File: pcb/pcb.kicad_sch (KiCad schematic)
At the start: 249 parts, among them J1 USB_C_Receptacle_USB2.0, J2 AVR-ISP-6, SW1 1U, SW10 1U, SW100 ISO SHIFT, SW101 2U, SW102 1.25U CTRL, SW103 1.25U GUI, SW104 1.25U ALT, SW105 6.25u SPACE, SW106 1U ALT, SW107 1U GUI, SW108 1U CTRL, SW109 1U, SW11 1U, SW110 1U, SW111 1U, SW112 1U, SW113 1U, SW114 1U, SW115 1.5U CTRL, SW116 1U GUI, SW117 1.5U ALT, SW118 7U SPACE, SW119 1.5U ALT, SW12 1U, SW120 1.5U CTRL, SW121 1.5U GUI, SW122 6U SPACE, SW123 SW_Push, SW124 SW_Push, SW13 1U, SW14 1U, SW15 1U, SW16 1U, SW17 1U, SW18 1U, SW19 1U, SW2 1U, SW20 1U, SW21 1U, SW22 1U, SW23 1U, SW24 1U, SW25 1U, SW26 1U, SW27 1U, SW28 1U, SW29 1U, SW3 1U, SW30 1U, SW31 1U, SW32 1U, SW33 1U, SW34 1U, SW35 1U, SW36 1U, SW37 2U, SW38 1U, SW39 1U, SW4 1U, SW40 1U, SW41 1U, SW42 1U, SW43 1.5U, SW44 1U, SW45 1U, SW46 1U, SW47 1U, SW48 1U, SW49 1U, SW5 1U, SW50 1U, SW51 1U, SW52 1U, SW53 1U, SW54 1U, SW55 1U, SW56 1.5U, SW57 1U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

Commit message: Finished first routing attempt
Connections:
- net COL0: now also U1.20 (PD6)
- net COL1: now also U1.19 (PD5)
- net COL2: now also U1.15 (PD1)
- net COL3: now also U1.14 (PD0)
- net COL4: now also U1.21 (PD7)
- net ROW0: now also U1.29 (PC7)
- net ROW1: now also U1.28 (PC6)
- net ROW10: now also D89.1 (K), U1.35 (PA5)
- net ROW11: now also U1.36 (PA4)
- net ROW12: now also U1.37 (PA3)
- net ROW2: now also U1.33 (PA7)
- net ROW3: now also U1.27 (PC5)
- net ROW4: now also U1.26 (PC4)
- net ROW5: now also U1.25 (PC3)
- net ROW6: now also U1.24 (PC2)
- net ROW7: now also U1.23 (PC1)
- net ROW8: now also U1.22 (PC0)
- net ROW9: now also U1.34 (PA6)
- net at SW94.1: now also D89.2 (A)
- no-connect marks 3 -> 7
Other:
- moved on the sheet: D89
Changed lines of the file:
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@@
   (junction (at 167.64 140.97) (diameter 0) (color 0 0 0 0)
   )
+  (no_connect (at 35.56 224.79))
+  (no_connect (at 33.02 224.79))
+  (no_connect (at 30.48 224.79))
+  (no_connect (at -177.165 242.57))
   (no_connect (at 200.66 265.43))
   (no_connect (at 45.72 255.27))
@@
     )
   )
+  (global_label "ROW9" (shape input) (at 45.72 224.79 90) (fields_autoplaced)
+    (effects (font (size 1.27 1.27)) (justify left))
+    (property "Intersheet References" "${INTERSHEET_REFS}" (id 0) (at 45.6406 217.1155 90)
+      (effects (font (size 1.27 1.27)) (justify left) hide)
+    )
+  )
   (global_label "SCK" (shape input) (at 71.12 224.79 90) (fields_autoplaced)
     (effects (font (size 1.27 1.27)) (justify left))
@@
     )
   )
-  (global_label "COL1" (shape input) (at 50.165 215.9 90) (fields_autoplaced)
+  (global_label "COL1" (shape input) (at 111.76 224.79 90) (fields_autoplaced)
     (effects (font (size 1.27 1.27)) (justify left))
-    (property "Intersheet References" "${INTERSHEET_REFS}" (id 0) (at 50.0856 208.6488 90)
+    (property "Intersheet References" "${INTERSHEET_REFS}" (id 0) (at 111.6806 217.5388 90)
       (effects (font (size 1.27 1.27)) (justify left) hide)
     )
@@
     )
   )
+  (global_label "ROW0" (shape input) (at 93.98 224.79 90) (fields_autoplaced)
+    (effects (font (size 1.27 1.27)) (justify left))
+    (property "Intersheet References" "${INTERSHEET_REFS}" (id 0) (at 93.9006 217.1155 90)
+      (effects (font (size 1.27 1.27)) (justify left) hide)
+    )
+  )
   (global_label "ROW3" (shape input) (at 72.39 80.01 180) (fields_autoplaced)
     (effects (font (size 0.635 0.635)) (justify right))
@@
     )
   )
+  (global_label "ROW12" (shape input) (at 38.1 224.79 90) (fields_autoplaced)
+    (effects (font (size 1.27 1.27)) (justify left))
+    (property "Intersheet References" "${INTERSHEET_REFS}" (id 0) (at 38.0206 215.9059 90)
+      (effects (font (size 1.27 1.27)) (justify left) hide)
+    )
+  )
+  (global_label "ROW10" (shape input) (at 43.18 224.79 90) (fields_autoplaced)
+    (effects (font (size 1.27 1.27)) (justify left))
+    (property "Intersheet References" "${INTERSHEET_REFS}" (id 0) (at 43.1006 215.9059 90)
+      (effects (font (size 1.27 1.27)) (justify left) hide)
+    )
+  )
+  (global_label "ROW5" (shape input) (at 83.82 224.79 90) (fields_autoplaced)
+    (effects (font (size 1.27 1.27)) (justify left))
+    (property "Intersheet References" "${INTERSHEET_REFS}" (id 0) (at 83.7406 217.1155 90)
+      (effects (font (size 1.27 1.27)) (justify left) hide)
+    )
+  )
+  (global_label "ROW2" (shape input) (at 48.26 224.79 90) (fields_autoplaced)
+    (effects (font (size 1.27 1.27)) (justify left))
+    (property "Intersheet References" "${INTERSHEET_REFS}" (id 0) (at 48.1806 217.1155 90)
+      (effects (font (size 1.27 1.27)) (justify left) hide)
+    )
+  )
+  (global_label "ROW7" (shape input) (at 78.74 224.79 90) (fields_autoplaced)
+    (effects (font (size 1.27 1.27)) (justify left))
+    (property "Intersheet References" "${INTERSHEET_REFS}" (id 0) (at 78.6606 217.1155 90)
+      (effects (font (size 1.27 1.27)) (justify left) hide)
+    )
+  )
   (global_label "ROW9" (shape input) (at 72.39 121.92 180) (fields_autoplaced)
     (effects (font (size 0.635 0.635)) (justify right))
@@
     )
   )
-  (global_label "COL4" (shape input) (at 42.545 215.9 90) (fields_autoplaced)
+  (global_label "COL4" (shape input) (at 116.84 224.79 90) (fields_autoplaced)
     (effects (font (size 1.27 1.27)) (justify left))
-    (property "Intersheet References" "${INTERSHEET_REFS}" (id 0) (at 42.4656 208.6488 90)
+    (property "Intersheet References" "${INTERSHEET_REFS}" (id 0) (at 116.7606 217.5388 90)
       (effects (font (size 1.27 1.27)) (justify left) hide)
     )
@@
     )
   )
-  (global_label "COL2" (shape input) (at 47.625 215.9 90) (fields_autoplaced)
+  (global_label "COL2" (shape input) (at 101.6 224.79 90) (fields_autoplaced)
     (effects (font (size 1.27 1.27)) (justify left))
-    (property "Intersheet References" "${INTERSHEET_REFS}" (id 0) (at 47.5456 208.6488 90)
+    (property "Intersheet References" "${INTERSHEET_REFS}" (id 0) (at 101.5206 217.5388 90)
       (effects (font (size 1.27 1.27)) (justify left) hide)
     )
@@
     )
   )
+  (global_label "ROW6" (shape input) (at 81.28 224.79 90) (fields_autoplaced)
+    (effects (font (size 1.27 1.27)) (justify left))
+    (property "Intersheet References" "${INTERSHEET_REFS}" (id 0) (at 81.2006 217.1155 90)
+      (effects (font (size 1.27 1.27)) (justify left) hide)
+    )
+  )
   (global_label "D+" (shape input) (at 242.57 252.73 0) (fields_autoplaced)
     (effects (font (size 1.27 1.27)) (justify left))
@@
     )
   )
+  (global_label "ROW1" (shape input) (at 91.44 224.79 90) (fields_autoplaced)
+    (effects (font (size 1.27 1.27)) (justify left))
+    (property "Intersheet References" "${INTERSHEET_REFS}" (id 0) (at 91.3606 217.1155 90)
+      (effects (font (size 1.27 1.27)) (justify left) hide)
+    )
+  )
   (global_label "SCK" (shape input) (at 287.02 252.73 0) (fields_autoplaced)
     (effects (font (size 1.27 1.27)) (justify left))
@@
     )
   )
+  (global_label "ROW11" (shape input) (at 40.64 224.79 90) (fields_autoplaced)
+    (effects (font (size 1.27 1.27)) (justify left))
+    (property "Intersheet References" "${INTERSHEET_REFS}" (id 0) (at 40.5606 215.9059 90)
+      (effects (font (size 1.27 1.27)) (justify left) hide)
+    )
+  )
   (global_label "ROW2" (shape input) (at 72.39 66.04 180) (fields_autoplaced)
     (effects (font (size 0.635 0.635)) (justify right))
@@
     )
   )
+  (global_label "ROW4" (shape input) (at 86.36 224.79 90) (fields_autoplaced)
+    (effects (font (size 1.27 1.27)) (justify left))
+    (property "Intersheet References" "${INTERSHEET_REFS}" (id 0) (at 86.2806 217.1155 90)
+      (effects (font (size 1.27 1.27)) (justify left) hide)
+    )
+  )
   (global_label "MISO" (shape input) (at 287.02 247.65 0) (fields_autoplaced)
     (effects (font (size 1.27 1.27)) (justify left))
@@
     )
   )
+  (global_label "ROW8" (shape input) (at 76.2 224.79 90) (fields_autoplaced)
+    (effects (font (size 1.27 1.27)) (justify left))
+    (property "Intersheet References" "${INTERSHEET_REFS}" (id 0) (at 76.1206 217.1155 90)
+      (effects (font (size 1.27 1.27)) (justify left) hide)
+    )
+  )
   (global_label "ROW12" (shape input) (at 72.39 137.16 180) (fields_autoplaced)
     (effects (font (size 0.635 0.635)) (justify right))
@@
     )
   )
+  (global_label "ROW3" (shape input) (at 88.9 224.79 90) (fields_autoplaced)
+    (effects (font (size 1.27 1.27)) (justify left))
+    (property "Intersheet References" "${INTERSHEET_REFS}" (id 0) (at 88.8206 217.1155 90)
+      (effects (font (size 1.27 1.27)) (justify left) hide)
+    )
+  )
   (global_label "BOOT" (shape input) (at 123.19 270.51 0) (fields_autoplaced)
     (effects (font (size 1.27 1.27)) (justify left))
@@
     )
   )
-  (global_label "COL0" (shape input) (at 52.705 215.9 90) (fields_autoplaced)
+  (global_label "COL0" (shape input) (at 114.3 224.79 90) (fields_autoplaced)
     (effects (font (size 1.27 1.27)) (justify left))
-    (property "Intersheet References" "${INTERSHEET_REFS}" (id 0) (at 52.6256 208.6488 90)
+    (property "Intersheet References" "${INTERSHEET_REFS}" (id 0) (at 114.2206 217.5388 90)
       (effects (font (size 1.27 1.27)) (justify left) hide)
     )
@@
     )
   )
-  (global_label "COL3" (shape input) (at 45.085 215.9 90) (fields_autoplaced)
+  (global_label "COL3" (shape input) (at 99.06 224.79 90) (fields_autoplaced)
     (effects (font (size 1.27 1.27)) (justify left))
-    (property "Intersheet References" "${INTERSHEET_REFS}" (id 0) (at 45.0056 208.6488 90)
+    (property "Intersheet References" "${INTERSHEET_REFS}" (id 0) (at 98.9806 217.5388 90)
       (effects (font (size 1.27 1.27)) (justify left) hide)
     )
@@
     (pin "2")
   )
-  (symbol (lib_id "Device:D_Small") (at 245.11 118.11 180) (unit 1)
+  (symbol (lib_id "Device:D_Small") (at 245.11 118.11 90) (unit 1)
     (in_bom yes) (on_board yes)
-    (property "Reference" "D89" (id 0) (at 241.935 116.205 90)
+    (property "Reference" "D89" (id 0) (at 247.015 114.935 90)
       (effects (font (size 0.635 0.635)) (justify right))
     )
-    (property "Value" "1N4148" (id 1) (at 243.205 116.205 90)
+    (property "Value" "1N4148" (id 1) (at 247.015 116.205 90)
       (effects (font (size 0.635 0.635)) (justify right))
     )

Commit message: Fixed 6u spacebar
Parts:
- C1: footprint Capacitor_THT:CP_Radial_D4.0mm_P1.50mm -> Capacitor_THT:C_Disc_D4.3mm_W1.9mm_P5.00mm
- SW122: footprint MX_Only:MXOnly-6U-ReversedStabilizers-NoLED -> MX_Only:MXOnly-6U-Centered-ReversedStabilizers-NoLED
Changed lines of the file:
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@@
       (effects (font (size 0.635 0.635)))
     )
-    (property "Footprint" "MX_Only:MXOnly-6U-ReversedStabilizers-NoLED" (id 2) (at 171.45 142.24 0)
+    (property "Footprint" "MX_Only:MXOnly-6U-Centered-ReversedStabilizers-NoLED" (id 2) (at 171.45 142.24 0)
       (effects (font (size 1.27 1.27)) hide)
     )
@@
       (effects (font (size 1.27 1.27)) (justify left))
     )
-    (property "Footprint" "Capacitor_THT:CP_Radial_D4.0mm_P1.50mm" (id 2) (at 54.61 265.43 0)
+    (property "Footprint" "Capacitor_THT:C_Disc_D4.3mm_W1.9mm_P5.00mm" (id 2) (at 54.61 265.43 0)
       (effects (font (size 1.27 1.27)) hide)
     )
@@
     )
     (path "/6691c87e-3d84-4222-a7d7-acc9c435d885"
-      (reference "C1") (unit 1) (value "4.7u") (footprint "Capacitor_THT:CP_Radial_D4.0mm_P1.50mm")
+      (reference "C1") (unit 1) (value "4.7u") (footprint "Capacitor_THT:C_Disc_D4.3mm_W1.9mm_P5.00mm")
     )
     (path "/0e3fa89d-d6e0-42c7-8c23-b39947577907"
@@
     )
     (path "/3d5d0f67-24dd-4ec0-a75c-164b57b95844"
-      (reference "SW122") (unit 1) (value "6U SPACE") (footprint "MX_Only:MXOnly-6U-ReversedStabilizers-NoLED")
+      (reference "SW122") (unit 1) (value "6U SPACE") (footprint "MX_Only:MXOnly-6U-Centered-ReversedStabilizers-NoLED")
     )
     (path "/fabae21c-0bf5-41e1-92c8-b0440c8cdf3c"

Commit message: PCB art, keyboard name under spacebar
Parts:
- C1: footprint Capacitor_THT:C_Disc_D4.3mm_W1.9mm_P5.00mm -> Capacitor_THT:C_Radial_D4.0mm_H7.0mm_P1.50mm
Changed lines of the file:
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@@
       (effects (font (size 1.27 1.27)) (justify left))
     )
-    (property "Footprint" "Capacitor_THT:C_Disc_D4.3mm_W1.9mm_P5.00mm" (id 2) (at 54.61 265.43 0)
+    (property "Footprint" "Capacitor_THT:C_Radial_D4.0mm_H7.0mm_P1.50mm" (id 2) (at 54.61 265.43 0)
       (effects (font (size 1.27 1.27)) hide)
     )
@@
     )
     (path "/6691c87e-3d84-4222-a7d7-acc9c435d885"
-      (reference "C1") (unit 1) (value "4.7u") (footprint "Capacitor_THT:C_Disc_D4.3mm_W1.9mm_P5.00mm")
+      (reference "C1") (unit 1) (value "4.7u") (footprint "Capacitor_THT:C_Radial_D4.0mm_H7.0mm_P1.50mm")
     )
     (path "/0e3fa89d-d6e0-42c7-8c23-b39947577907"

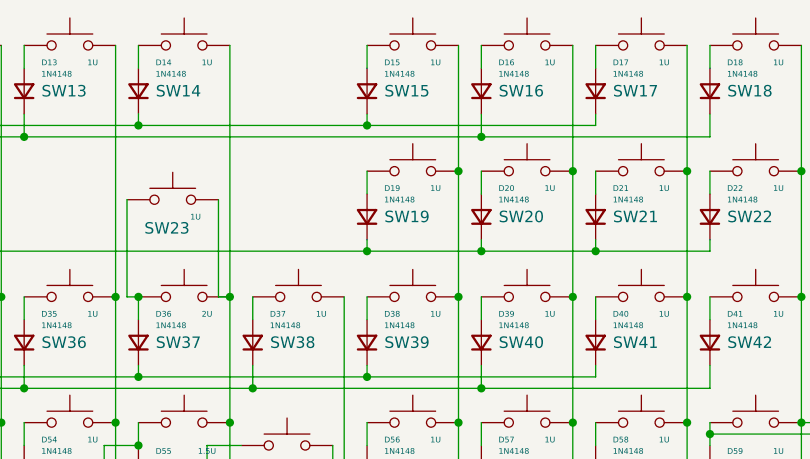
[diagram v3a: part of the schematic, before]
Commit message: Reroute ROW2 switches
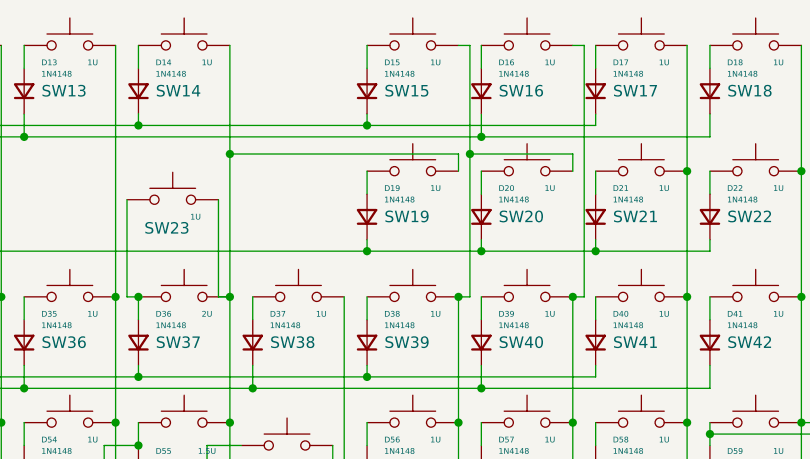
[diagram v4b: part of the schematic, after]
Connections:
- net COL6: now also SW19.2
- net COL7: now also SW20.2; no longer SW19.2
- net COL8: no longer SW20.2
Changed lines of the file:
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@@
   (junction (at 255.27 166.37) (diameter 0) (color 0 0 0 0)
   )
+  (junction (at 306.07 71.12) (diameter 0) (color 0 0 0 0)
+  )
   (junction (at 194.31 95.25) (diameter 0) (color 0 0 0 0)
   )
@@
   (junction (at 200.66 252.73) (diameter 0) (color 0 0 0 0)
   )
+  (junction (at 267.97 55.245) (diameter 0) (color 0 0 0 0)
+  )
   (junction (at 194.31 123.19) (diameter 0) (color 0 0 0 0)
   )
@@
   (junction (at 293.37 99.06) (diameter 0) (color 0 0 0 0)
   )
+  (junction (at 293.37 71.12) (diameter 0) (color 0 0 0 0)
+  )
   (junction (at 261.62 99.06) (diameter 0) (color 0 0 0 0)
   )
@@
   (junction (at 179.07 134.62) (diameter 0) (color 0 0 0 0)
   )
-  (junction (at 306.07 71.12) (diameter 0) (color 0 0 0 0)
-  )
   (junction (at 257.81 71.12) (diameter 0) (color 0 0 0 0)
   )
@@
   (junction (at 280.67 127) (diameter 0) (color 0 0 0 0)
   )
-  (junction (at 306.07 57.15) (diameter 0) (color 0 0 0 0)
-  )
   (junction (at 105.41 127) (diameter 0) (color 0 0 0 0)
   )
@@
   (junction (at 217.17 113.03) (diameter 0) (color 0 0 0 0)
   )
+  (junction (at 294.64 55.245) (diameter 0) (color 0 0 0 0)
+  )
   (junction (at 229.87 71.12) (diameter 0) (color 0 0 0 0)
   )
@@
   (junction (at 204.47 71.12) (diameter 0) (color 0 0 0 0)
   )
-  (junction (at 293.37 71.12) (diameter 0) (color 0 0 0 0)
-  )
   (junction (at 267.97 85.09) (diameter 0) (color 0 0 0 0)
   )
@@
   )
   (junction (at 177.8 140.97) (diameter 0) (color 0 0 0 0)
-  )
-  (junction (at 293.37 57.15) (diameter 0) (color 0 0 0 0)
   )
   (junction (at 181.61 121.92) (diameter 0) (color 0 0 0 0)
@@
     (stroke (width 0) (type default) (color 0 0 0 0))
   )
-  (wire (pts (xy 306.07 43.18) (xy 306.07 57.15))
-    (stroke (width 0) (type default) (color 0 0 0 0))
-  )
   (wire (pts (xy 308.61 85.09) (xy 308.61 87.63))
     (stroke (width 0) (type default) (color 0 0 0 0))
@@
     (stroke (width 0) (type default) (color 0 0 0 0))
   )
+  (wire (pts (xy 307.34 71.12) (xy 306.07 71.12))
+    (stroke (width 0) (type default) (color 0 0 0 0))
+  )
   (wire (pts (xy 228.6 134.62) (xy 228.6 140.97))
     (stroke (width 0) (type default) (color 0 0 0 0))
@@
     (stroke (width 0) (type default) (color 0 0 0 0))
   )
+  (wire (pts (xy 306.07 43.18) (xy 307.34 43.18))
+    (stroke (width 0) (type default) (color 0 0 0 0))
+  )
   (wire (pts (xy 229.87 99.06) (xy 229.87 113.03))
     (stroke (width 0) (type default) (color 0 0 0 0))
@@
     (stroke (width 0) (type default) (color 0 0 0 0))
   )
+  (wire (pts (xy 293.37 55.245) (xy 267.97 55.245))
+    (stroke (width 0) (type default) (color 0 0 0 0))
+  )
   (wire (pts (xy 153.67 113.03) (xy 153.67 161.29))
     (stroke (width 0) (type default) (color 0 0 0 0))
@@
     (stroke (width 0) (type default) (color 0 0 0 0))
   )
+  (wire (pts (xy 294.64 43.18) (xy 293.37 43.18))
+    (stroke (width 0) (type default) (color 0 0 0 0))
+  )
   (wire (pts (xy 118.11 270.51) (xy 123.19 270.51))
     (stroke (width 0) (type default) (color 0 0 0 0))
@@
     (stroke (width 0) (type default) (color 0 0 0 0))
   )
-  (wire (pts (xy 293.37 43.18) (xy 293.37 57.15))
-    (stroke (width 0) (type default) (color 0 0 0 0))
-  )
   (wire (pts (xy 295.91 134.62) (xy 295.91 137.16))
     (stroke (width 0) (type default) (color 0 0 0 0))
@@
     (stroke (width 0) (type default) (color 0 0 0 0))
   )
+  (wire (pts (xy 294.64 55.245) (xy 306.07 55.245))
+    (stroke (width 0) (type default) (color 0 0 0 0))
+  )
   (wire (pts (xy 156.21 92.71) (xy 156.21 93.98))
     (stroke (width 0) (type default) (color 0 0 0 0))
@@
     (stroke (width 0) (type default) (color 0 0 0 0))
   )
+  (wire (pts (xy 293.37 71.12) (xy 294.64 71.12))
+    (stroke (width 0) (type default) (color 0 0 0 0))
+  )
   (wire (pts (xy 143.51 85.09) (xy 143.51 87.63))
     (stroke (width 0) (type default) (color 0 0 0 0))
@@
     (stroke (width 0) (type default) (color 0 0 0 0))
   )
+  (wire (pts (xy 307.34 43.18) (xy 307.34 71.12))
+    (stroke (width 0) (type default) (color 0 0 0 0))
+  )
   (wire (pts (xy 224.79 250.19) (xy 234.95 250.19))
     (stroke (width 0) (type default) (color 0 0 0 0))
@@
     (stroke (width 0) (type default) (color 0 0 0 0))
   )
-  (wire (pts (xy 293.37 57.15) (xy 293.37 71.12))
-    (stroke (width 0) (type default) (color 0 0 0 0))
-  )
   (wire (pts (xy 143.51 43.18) (xy 143.51 45.72))
     (stroke (width 0) (type default) (color 0 0 0 0))
@@
     (stroke (width 0) (type default) (color 0 0 0 0))
   )
+  (wire (pts (xy 267.97 55.245) (xy 267.97 71.12))
+    (stroke (width 0) (type default) (color 0 0 0 0))
+  )
   (wire (pts (xy 127 160.02) (xy 140.97 160.02))
     (stroke (width 0) (type default) (color 0 0 0 0))
@@
     (stroke (width 0) (type default) (color 0 0 0 0))
   )
+  (wire (pts (xy 294.64 71.12) (xy 294.64 55.245))
+    (stroke (width 0) (type default) (color 0 0 0 0))
+  )
   (wire (pts (xy 308.61 99.06) (xy 308.61 101.6))
     (stroke (width 0) (type default) (color 0 0 0 0))
@@
     (stroke (width 0) (type default) (color 0 0 0 0))
   )
-  (wire (pts (xy 306.07 57.15) (xy 306.07 71.12))
-    (stroke (width 0) (type default) (color 0 0 0 0))
-  )
   (wire (pts (xy 331.47 113.03) (xy 331.47 127))
     (stroke (width 0) (type default) (color 0 0 0 0))
@@
     (stroke (width 0) (type default) (color 0 0 0 0))
   )
+  (wire (pts (xy 294.64 55.245) (xy 294.64 43.18))
+    (stroke (width 0) (type default) (color 0 0 0 0))
+  )
   (wire (pts (xy 105.41 78.74) (xy 105.41 80.01))
     (stroke (width 0) (type default) (color 0 0 0 0))
@@
     (stroke (width 0) (type default) (color 0 0 0 0))
   )
-  (wire (pts (xy 267.97 43.18) (xy 267.97 71.12))
+  (wire (pts (xy 267.97 43.18) (xy 267.97 55.245))
     (stroke (width 0) (type default) (color 0 0 0 0))
   )
@@
     (stroke (width 0) (type default) (color 0 0 0 0))
   )
+  (wire (pts (xy 293.37 57.15) (xy 293.37 55.245))
+    (stroke (width 0) (type default) (color 0 0 0 0))
+  )
   (wire (pts (xy 321.31 113.03) (xy 321.31 114.3))
     (stroke (width 0) (type default) (color 0 0 0 0))
@@
     (stroke (width 0) (type default) (color 0 0 0 0))
   )
+  (wire (pts (xy 306.07 55.245) (xy 306.07 57.15))
+    (stroke (width 0) (type default) (color 0 0 0 0))
+  )

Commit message: Replaced switch footprints
Need to still add the correct 6u spacebar footprint
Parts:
- SW1, SW10, SW106, SW107, SW108, SW109, SW11, SW110, SW111, SW112, SW113, SW114, SW116, SW12, SW13, SW14, SW15, SW16, SW17, SW18, SW19, SW2, SW20, SW21, SW22, SW23, SW24, SW25, SW26, SW27, SW28, SW29, SW3, SW30, SW31, SW32, SW33, SW34, SW35, SW36, SW38, SW39, SW4, SW40, SW41, SW42, SW44, SW45, SW46, SW47, SW48, SW49, SW5, SW50, SW51, SW52, SW53, SW54, SW55, SW57, SW58, SW59, SW6, SW60, SW64, SW65, SW66, SW67, SW68, SW69, SW7, SW70, SW71, SW72, SW73, SW74, SW76, SW77, SW78, SW79, SW8, SW81, SW83, SW84, SW85, SW86, SW87, SW88, SW89, SW9, SW90, SW91, SW92, SW93, SW95, SW96, SW97, SW98, SW99: footprint MX_Only:MXOnly-1U-NoLED -> 0xcb:SW_Cherry_MX_PCB_1.00u
- SW100, SW102, SW103, SW104, SW80: footprint MX_Only:MXOnly-1.25U-NoLED -> 0xcb:SW_Cherry_MX_PCB_1.25u
- SW101, SW61: footprint MX_Only:MXOnly-2U-ReversedVerticalStabilizers-NoLED -> 0xcb:SW_Cherry_MX_PCB_2.00u
- SW105: footprint MX_Only:MXOnly-6.25U-ReversedStabilizers-NoLED -> 0xcb:SW_Cherry_MX_PCB_6.25u
- SW115, SW117, SW119, SW120, SW121, SW43, SW56: footprint MX_Only:MXOnly-1.5U-NoLED -> 0xcb:SW_Cherry_MX_PCB_1.50u
- SW118: footprint MX_Only:MXOnly-7U-ReversedStabilizers-NoLED -> 0xcb:SW_Cherry_MX_PCB_7.00u
- SW122: footprint MX_Only:MXOnly-6U-Centered-ReversedStabilizers-NoLED -> 0xcb:SW_Cherry_MX_PCB_3.00u
- SW37: footprint MX_Only:MXOnly-2U-NoLED -> 0xcb:SW_Cherry_MX_PCB_2.00u
- SW62: footprint MX_Only:MXOnly-ISO-ReversedStabilizers-NoLED -> 0xcb:SW_Cherry_MX_PCB_ISOEnter_Rotated90
- SW63, SW94: footprint MX_Only:MXOnly-1.75U-NoLED -> 0xcb:SW_Cherry_MX_PCB_1.75u
- SW75, SW82: footprint MX_Only:MXOnly-2.25U-ReversedStabilizers-NoLED -> 0xcb:SW_Cherry_MX_PCB_2.25u

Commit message: Added capacitor polarity marking
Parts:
- C1: footprint Capacitor_THT:C_Radial_D4.0mm_H7.0mm_P1.50mm -> Capacitor_THT:CP_Radial_D4.0mm_P1.50mm
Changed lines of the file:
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@@
       (effects (font (size 1.27 1.27)) (justify left))
     )
-    (property "Footprint" "Capacitor_THT:C_Radial_D4.0mm_H7.0mm_P1.50mm" (id 2) (at 54.61 265.43 0)
+    (property "Footprint" "Capacitor_THT:CP_Radial_D4.0mm_P1.50mm" (id 2) (at 54.61 265.43 0)
       (effects (font (size 1.27 1.27)) hide)
     )
@@
     )
     (path "/6691c87e-3d84-4222-a7d7-acc9c435d885"
-      (reference "C1") (unit 1) (value "4.7u") (footprint "Capacitor_THT:C_Radial_D4.0mm_H7.0mm_P1.50mm")
+      (reference "C1") (unit 1) (value "4.7u") (footprint "Capacitor_THT:CP_Radial_D4.0mm_P1.50mm")
     )
     (path "/0e3fa89d-d6e0-42c7-8c23-b39947577907"
